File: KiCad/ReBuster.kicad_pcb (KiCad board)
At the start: 4 copper layers, 38 x 38 mm, 36 parts, among them U1 10M02SCU169C8G, U2 LM1117-3.3, U3 SN74CBTD16210, U4 SN74CBTD16210, U5 SN74CBTD16210, U6 SN74CBTD16210, U7 PLCC_84_plug, U8 PLCC_84_plug

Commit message: small GND fix improvement for C22,C24 adding a second GND via
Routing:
- net GND: vias 44 -> 46

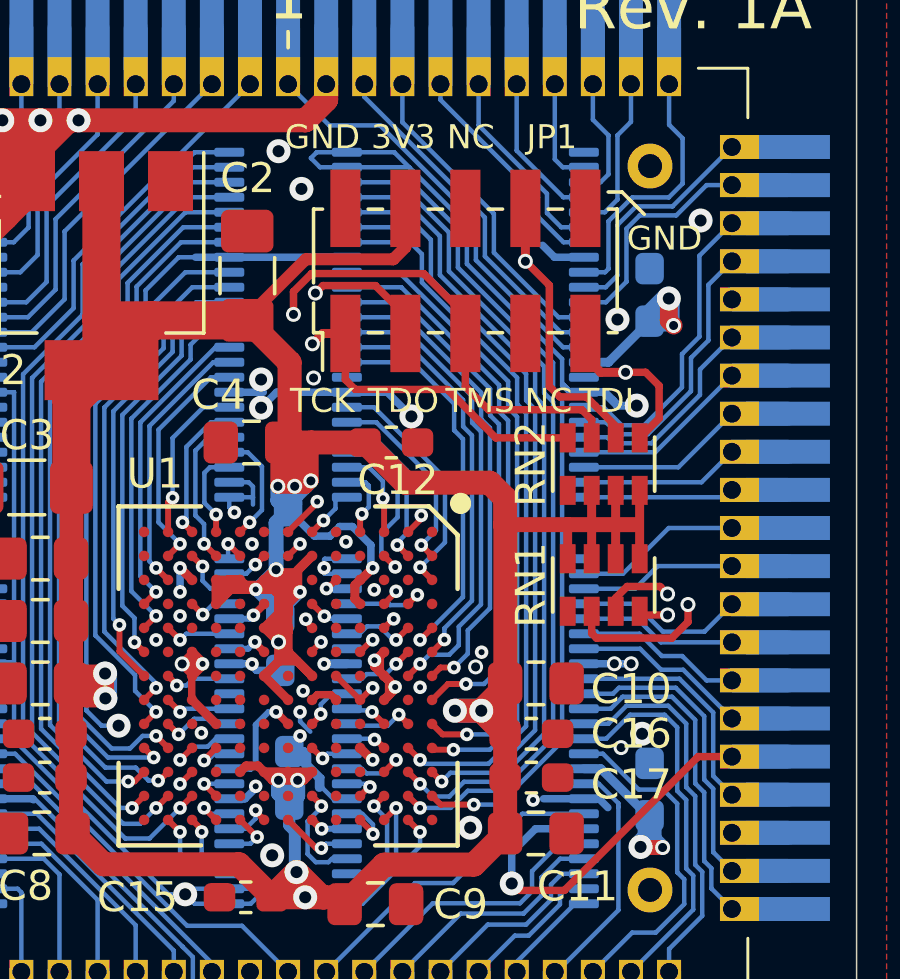
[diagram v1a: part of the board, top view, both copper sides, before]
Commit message: small routing improvement
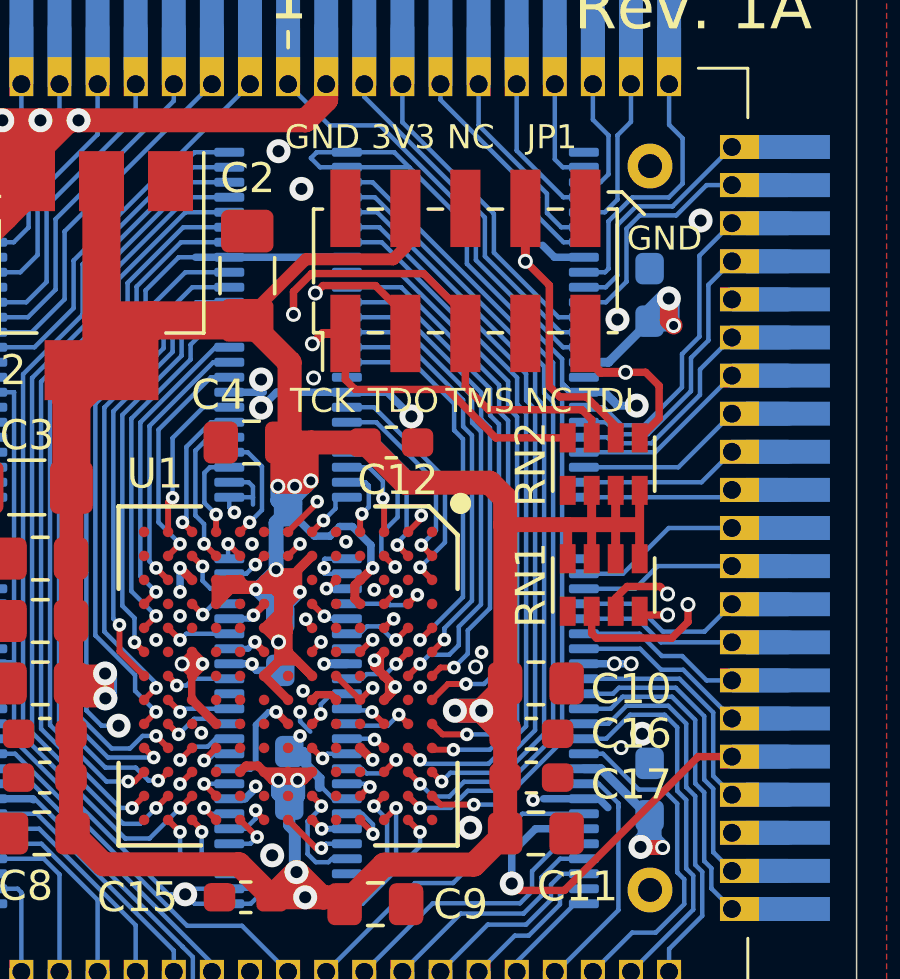
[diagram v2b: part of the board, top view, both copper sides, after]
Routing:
- net EBR4_FPGA: track 25.0 -> 24.3 mm
- net EBR1_FPGA: track 27.2 -> 26.4 mm
- net EBR3_FPGA: track 28.1 -> 27.4 mm
- net EBR2_FPGA: track 28.2 -> 27.4 mm
- net EBR0_FPGA: track 24.5 -> 24.0 mm

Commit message: Change RN1, RN2 value from 10k to 4.7k (CAY16A-4701F4LF) to follow Gowin JTAG recommended design.
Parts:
- RN1, RN2: value 10k -> 4.7k
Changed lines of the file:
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@@
       (effects (font (size 1 1) (thickness 0.15)))
     )
-    (fp_text value 10k (at 12.37 2.665 90) (layer F.Fab)
+    (fp_text value 4.7k (at 12.37 2.665 90) (layer F.Fab)
       (effects (font (size 1 1) (thickness 0.015)))
     )
@@
       (effects (font (size 1 1) (thickness 0.15)))
     )
-    (fp_text value 10k (at 12.37 2.665 90) (layer F.Fab)
+    (fp_text value 4.7k (at 12.37 2.665 90) (layer F.Fab)
       (effects (font (size 1 1) (thickness 0.015)))
     )

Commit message: Change U1 from 10M02SCU169C8G to pin compatible Gowin FPGA GW1N-UV9UG169C6/I5
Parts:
- U1: value 10M02SCU169C8G -> GW1N-UV9UG169C6/I5
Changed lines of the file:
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@@
       (effects (font (size 1 1) (thickness 0.15)))
     )
-    (fp_text value 10M02SCU169C8G (at 0 6.5 90) (layer F.Fab) hide
+    (fp_text value "GW1N-UV9UG169C6/I5 " (at 0 6.5 90) (layer F.Fab) hide
       (effects (font (size 1 1) (thickness 0.15)))
     )

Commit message: Change back to a 10M02SCU169 FPGA
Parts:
- U1: value GW1N-UV9UG169C6/I5 -> 10M02SCU169

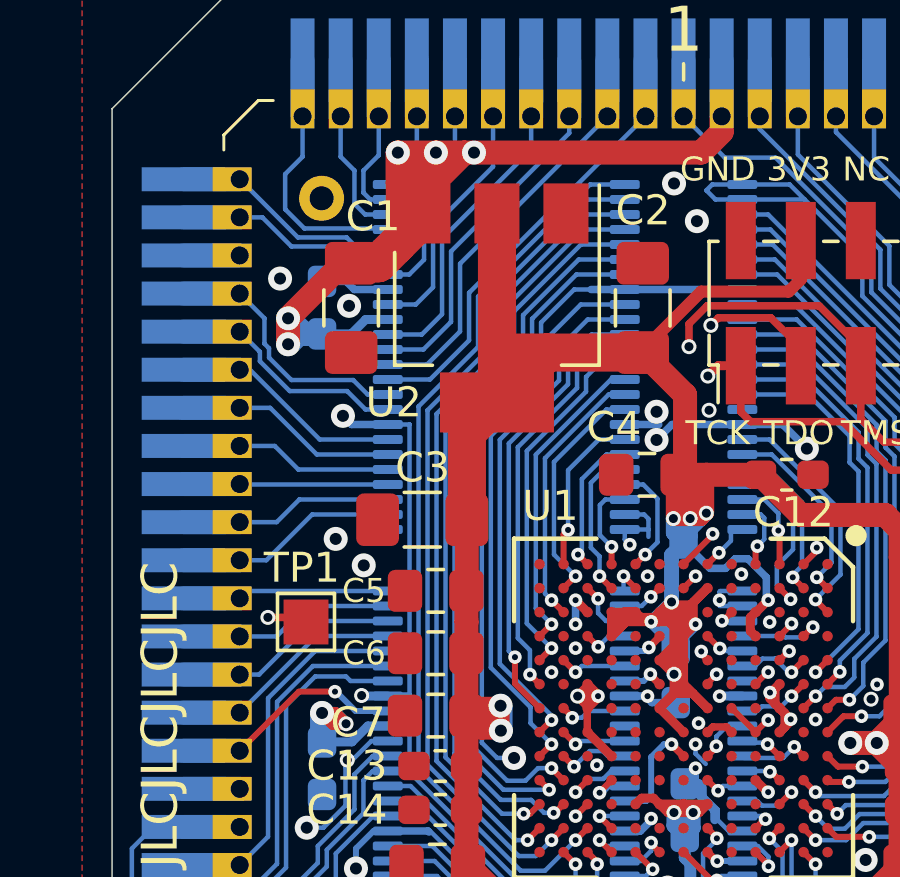
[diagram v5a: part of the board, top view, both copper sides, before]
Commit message: replace U4 (SN74CBTD16210) with a SN74LVC16T245DGVR
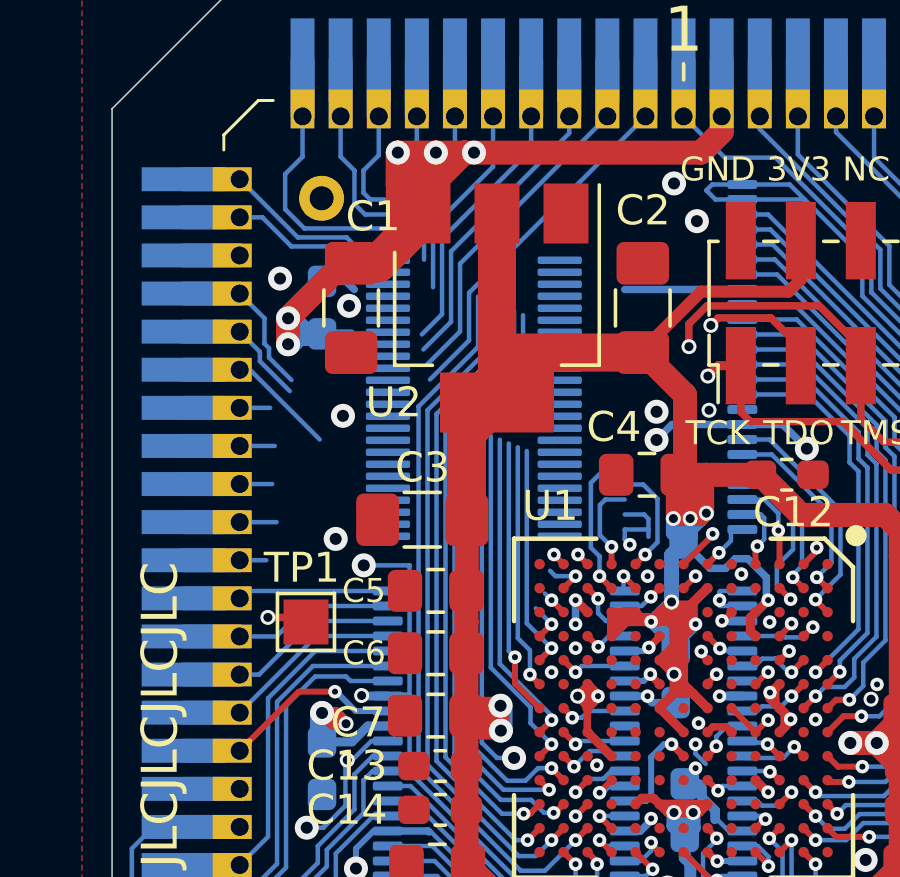
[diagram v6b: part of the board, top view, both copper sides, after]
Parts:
- U4: value SN74CBTD16210 -> SN74LVC16T245DGVR; footprint ReBuster:TSSOP-48_6.1x12.5mm_P0.5mm_padLength_1mm -> Package_SO:TSSOP-48_4.4x9.7mm_P0.4mm
- moved U4 1.75 mm to (137.5, 69.1)
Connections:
- net /NC2 renamed Net-(U4-Pad1)
- U4 pad 10: RMC -> GND
- U4 pad 11: CCS -> Net-(U4-Pad11)
- U4 pad 12: A2 -> Net-(U4-Pad12)
- U4 pad 13: A1 -> Net-(U4-Pad13)
- U4 pad 14: A0 -> Net-(U4-Pad14)
- U4 pad 15: VCC -> GND
- U4 pad 16: RW -> Net-(U4-Pad16)
- U4 pad 17: GND -> Net-(U4-Pad17)
- U4 pad 18: SIZ0 -> Net-(U4-Pad18)
- U4 pad 19: STERM -> Net-(U4-Pad19)
- U4 pad 2: WAIT -> Net-(U4-Pad2)
- U4 pad 20: DSACK1 -> Net-(U4-Pad20)
- U4 pad 21: DSACK0 -> GND
- U4 pad 22: DS -> Net-(U4-Pad22)
- U4 pad 23: AS -> Net-(U4-Pad23)
- U4 pad 24: SIZ1 -> Net-(U4-Pad24)
- U4 pad 25: SIZ1_FPGA -> Net-(U4-Pad25)
- U4 pad 26: AS_FPGA -> Net-(U4-Pad26)
- U4 pad 27: DS_FPGA -> Net-(U4-Pad27)
- U4 pad 28: DSACK0_FPGA -> GND
- U4 pad 29: DSACK1_FPGA -> Net-(U4-Pad29)
- U4 pad 3: DOE -> Net-(U4-Pad3)
- U4 pad 30: STERM_FPGA -> Net-(U4-Pad30)
- U4 pad 31: SIZ0_FPGA -> Net-(U4-Pad31)
- U4 pad 32: GND -> Net-(U4-Pad32)
- U4 pad 33: RW_FPGA -> Net-(U4-Pad33)
- U4 pad 34: A0_FPGA -> GND
- U4 pad 35: A1_FPGA -> Net-(U4-Pad35)
- U4 pad 36: A2_FPGA -> Net-(U4-Pad36)
- U4 pad 37: CCS_FPGA -> Net-(U4-Pad37)
- U4 pad 38: RMC_FPGA -> Net-(U4-Pad38)
- U4 pad 39: SBR_FPGA -> GND
- U4 pad 4: DTACK -> GND
- U4 pad 40: SBG_FPGA -> Net-(U4-Pad40)
- U4 pad 41: GND -> Net-(U4-Pad41)
- U4 pad 42: CIIN_FPGA -> Net-(U4-Pad42)
- U4 pad 43: MTACK_FPGA -> Net-(U4-Pad43)
- U4 pad 44: DTACK_FPGA -> Net-(U4-Pad44)
- U4 pad 45: DOE_FPGA -> GND
- U4 pad 46: WAIT_FPGA -> Net-(U4-Pad46)
- U4 pad 47: GND -> Net-(U4-Pad47)
- U4 pad 48: GND -> Net-(U4-Pad48)
- U4 pad 5: MTACK -> Net-(U4-Pad5)
- U4 pad 6: CIIN -> Net-(U4-Pad6)
- U4 pad 7: SBG -> Net-(U4-Pad7)
- U4 pad 8: GND -> Net-(U4-Pad8)
- U4 pad 9: SBR -> Net-(U4-Pad9)
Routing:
- net GND: track 133.1 -> 106.0 mm, vias 46 -> 45
- net Net-(U9-Pad30): track 0.00 -> 11.6 mm, vias 0 -> 1
- net RMC_FPGA: track 10.4 -> 1.31 mm
- net SIZ0_FPGA: track 22.6 -> 14.4 mm
- net SBR_FPGA: track 8.93 -> 0.88 mm
- net RW_FPGA: track 18.8 -> 11.7 mm
- net A0_FPGA: track 17.1 -> 10.6 mm
- net SIZ1_FPGA: track 30.6 -> 24.2 mm
- net SBG_FPGA: track 7.75 -> 1.49 mm
- net AS_FPGA: track 28.5 -> 22.5 mm
- net A1_FPGA: track 15.1 -> 9.25 mm
- net DS_FPGA: track 26.3 -> 20.7 mm
- net A2_FPGA: track 13.5 -> 8.20 mm
- net DSACK0_FPGA: track 24.9 -> 19.9 mm
- net CIIN_FPGA: track 5.51 -> 0.45 mm
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
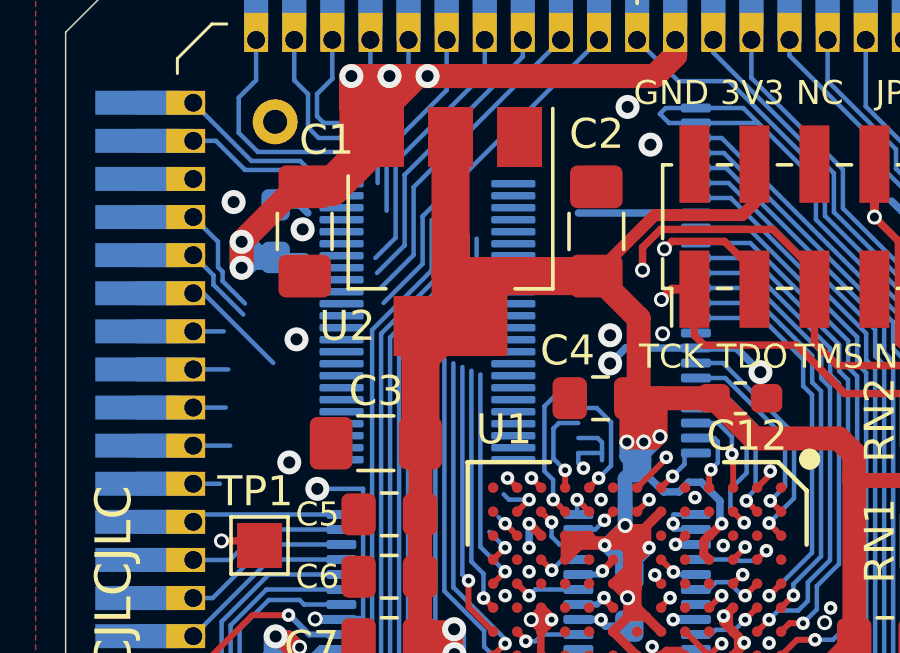
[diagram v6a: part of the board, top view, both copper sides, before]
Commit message: Fix pad size on U4 footprint
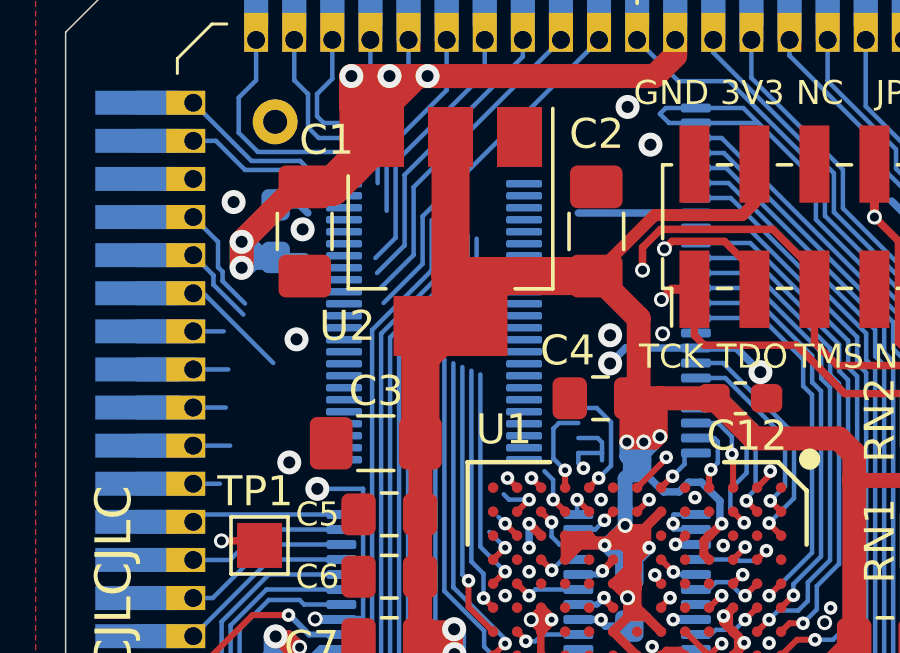
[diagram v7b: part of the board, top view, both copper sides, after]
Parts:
- moved U4 0.22 mm to (137.7, 69.1)
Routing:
- net DTACK_FPGA: track 5.11 -> 1.64 mm

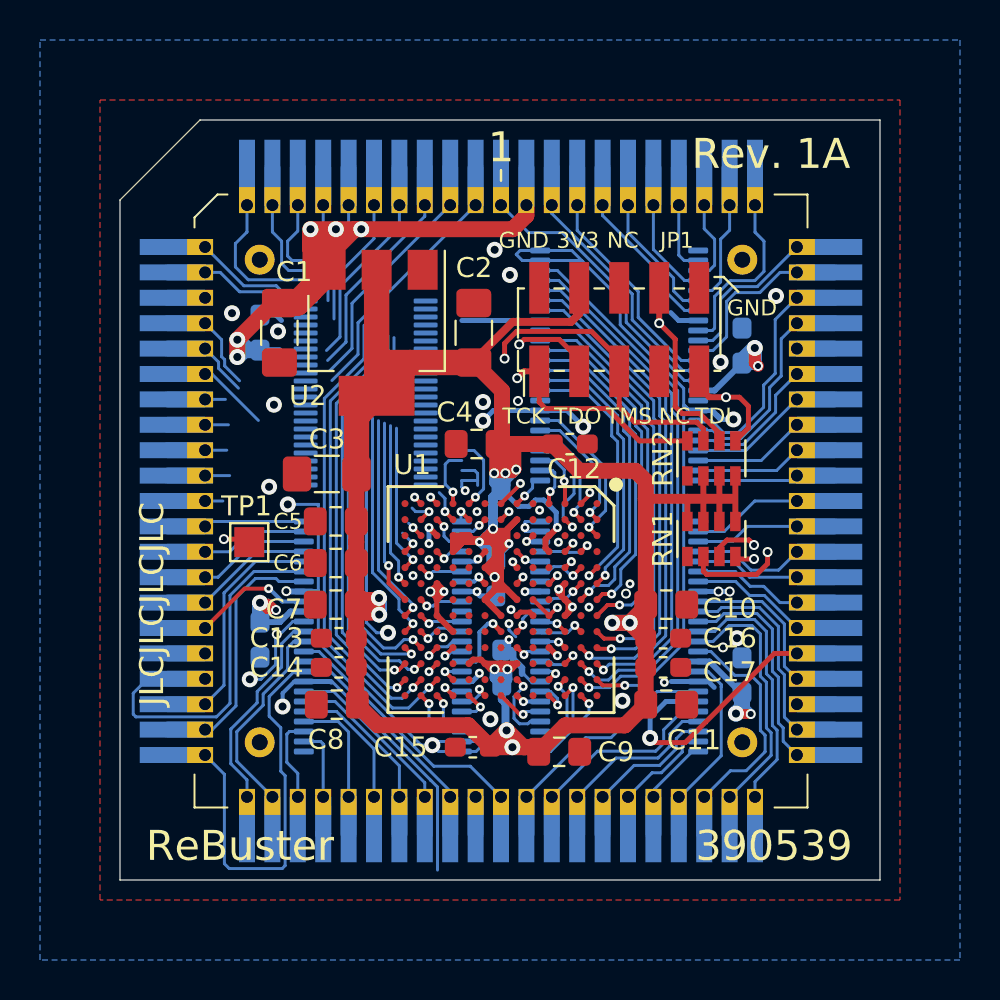
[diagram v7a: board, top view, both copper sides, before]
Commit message: Add 74LVC2T45DC for handling DTACKn and MTACKn
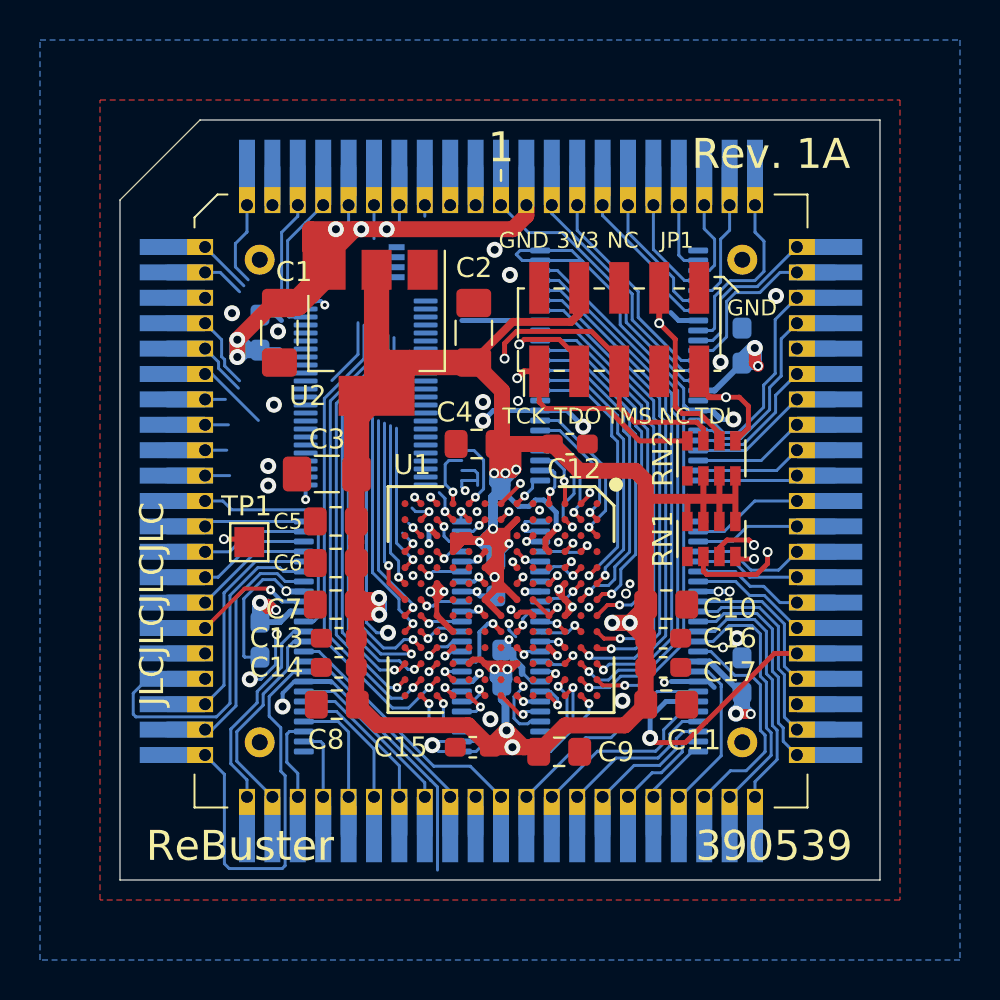
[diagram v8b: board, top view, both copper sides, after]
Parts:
- added U7: 74LVC2T45DC, Package_SO:VSSOP-8_2.3x2mm_P0.5mm, B.Cu at (137.7, 62.5)
- renumbered U7 to U8, U8 to U9
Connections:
- U1 pad H8: Net-(U1-PadH8) -> WAIT_FPGA
- U1 pad K1: WAIT_FPGA -> Net-(U1-PadK1)
- U4 pad 1: Net-(U4-Pad1) -> DIR_U4
- U4 pad 18: Net-(U4-Pad18) -> VCC
- U4 pad 22: Net-(U4-Pad22) -> AS
- U4 pad 23: Net-(U4-Pad23) -> SIZ1
- U4 pad 24: Net-(U4-Pad24) -> DIR_U4
- U4 pad 25: Net-(U4-Pad25) -> OE
- U4 pad 26: Net-(U4-Pad26) -> SIZ1_FPGA
- U4 pad 27: Net-(U4-Pad27) -> AS_FPGA
- U4 pad 31: Net-(U4-Pad31) -> 3V3
- U4 pad 42: Net-(U4-Pad42) -> 3V3
- U4 pad 48: Net-(U4-Pad48) -> OE
- U4 pad 7: Net-(U4-Pad7) -> VCC
- U6 pad 14: GND -> WAIT
- U6 pad 34: Net-(U6-Pad34) -> WAIT_FPGA
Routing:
- net GND: track 106.0 -> 93.0 mm
- net WAIT: track 2.76 -> 13.7 mm
- net A2: track 12.6 -> 1.87 mm
- net A1: track 11.7 -> 2.43 mm
- net CCS: track 13.6 -> 5.30 mm
- net A0: track 10.6 -> 3.38 mm
- net RW: track 8.39 -> 3.54 mm
- net DS: track 6.23 -> 1.87 mm
- net SIZ1: track 4.97 -> 8.58 mm
- net SIZ0: track 7.07 -> 3.56 mm
- net AS: track 5.53 -> 8.78 mm
- net DSACK1: track 7.70 -> 4.61 mm
- net Net-(U1-PadK1): track 0.00 -> 3.04 mm, vias 0 -> 1
- net DSACK0: track 8.90 -> 6.11 mm
- net STERM: track 6.32 -> 3.99 mm
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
